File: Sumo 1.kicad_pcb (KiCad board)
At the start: 2 copper layers, 96.5 x 61 mm, 17 parts, among them J1 Trinket_Pro_5V, J2 SENSOR_CONN, J3 SENSOR_CONN, J4 SENSOR_CONN, M1 Motor_Connection, M2 Motor_Connection, M3 Motor_Connection, M4 Motor_Connection, U1 TB6612FNG

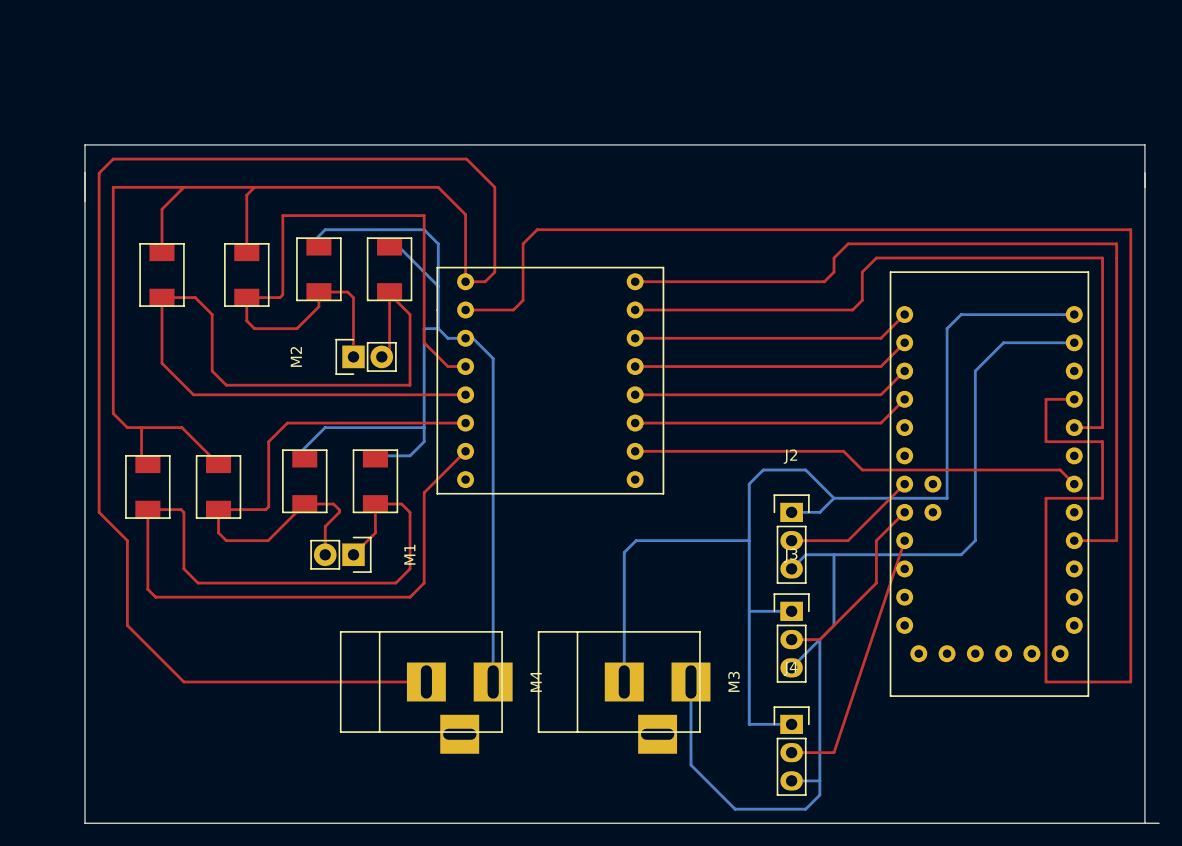
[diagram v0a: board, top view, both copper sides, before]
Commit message: First spin using bare SMT TB6612FNG.
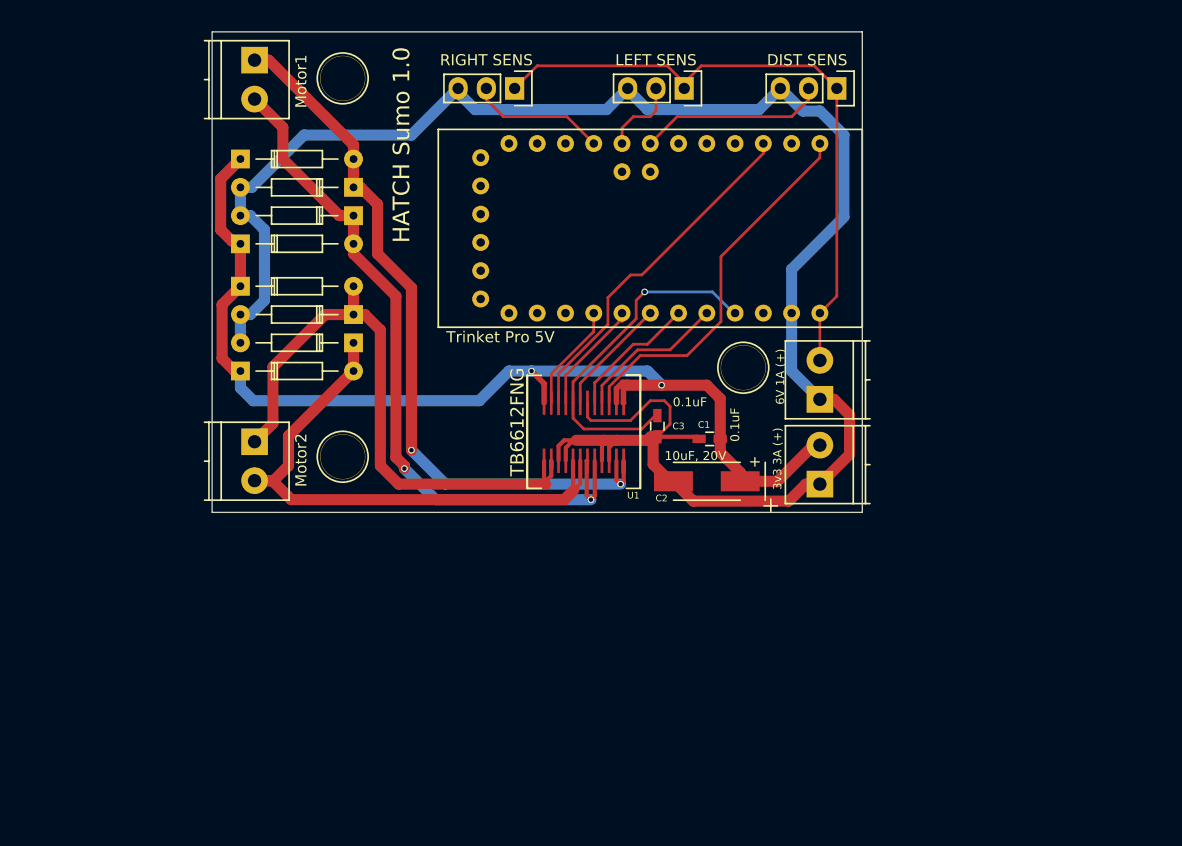
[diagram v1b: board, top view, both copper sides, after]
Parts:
- added ?: , Connect:1pin, F.Cu at (140.0, 122.0)
- added ?: , Connect:1pin, F.Cu at (176.0, 114.0)
- added ?: , Connect:1pin, F.Cu at (140.0, 88.0)
- added C1: 0.1uF, Capacitors_SMD:C_0603_HandSoldering, F.Cu at (173.0, 120.4)
- added C2: 10uF, 20V, Capacitors_Tantalum_SMD:TantalC_SizeC_EIA-6032_HandSoldering, F.Cu at (172.7, 124.2)
- added C3: 0.1uF, Capacitors_SMD:C_0603_HandSoldering, F.Cu at (168.3, 119.3)
- D1, D2, D3, D4, D5, D6, D7, D8: value D_Small -> 1N4001; footprint ArduinoFootprints:S1BB_rectifier_diode -> Diodes_ThroughHole:Diode_DO-35_SOD27_Horizontal_RM10
- J1: value Trinket_Pro_5V -> DIST SENS; footprint ArduinoFootprints:Trinket_Pro_5V -> Pin_Headers:Pin_Header_Straight_1x03
- J2: value SENSOR_CONN -> LEFT SENS
- J3: value SENSOR_CONN -> RIGHT SENS
- J4: value SENSOR_CONN -> Trinket Pro 5V; footprint Pin_Headers:Pin_Header_Straight_1x03 -> ArduinoFootprints:Trinket_Pro_5V
- M1: value Motor_Connection -> Logic Power; footprint Pin_Headers:Pin_Header_Straight_1x02 -> Terminal_Blocks:TerminalBlock_Pheonix_PT-3.5mm_2pol
- M2: value Motor_Connection -> Motor Power; footprint Pin_Headers:Pin_Header_Straight_1x02 -> Terminal_Blocks:TerminalBlock_Pheonix_PT-3.5mm_2pol
- M3: value Motor_Connection -> Motor1; footprint Connect:BARREL_JACK -> Terminal_Blocks:TerminalBlock_Pheonix_PT-3.5mm_2pol
- M4: value Motor_Connection -> Motor2; footprint Connect:BARREL_JACK -> Terminal_Blocks:TerminalBlock_Pheonix_PT-3.5mm_2pol
- U1: footprint ArduinoFootprints:TB6612FNG_motor_driver -> ArduinoFootprints:TB6612FNG
- moved M3 64.9 mm to (132.1, 86.4), turned to 270 degrees
- moved J4 53.8 mm to (186.7, 92.6), turned to 270 degrees
- moved J3 53.2 mm to (155.4, 88.9), turned to 270 degrees
- moved M1 44.2 mm to (182.9, 116.8), turned to 90 degrees
- moved M2 43.4 mm to (182.9, 124.5)
- moved J2 39.3 mm to (170.7, 88.9), turned to 270 degrees
- moved D2 29.2 mm to (141.0, 97.8), turned to 180 degrees
- moved D1 27.4 mm to (130.8, 95.2), turned to 0 degrees
- moved D4 27.4 mm to (141.0, 100.3), turned to 180 degrees
- moved M4 26.4 mm to (132.1, 120.7), turned to 270 degrees
- moved U1 19.8 mm to (161.7, 119.8)
- moved D3 19.0 mm to (130.8, 102.9), turned to 0 degrees
- moved J1 17.2 mm to (184.4, 88.9), turned to 270 degrees
- moved D7 12.5 mm to (130.8, 114.3), turned to 0 degrees
- moved D6 5.24 mm to (141.0, 109.2), turned to 180 degrees
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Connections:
- J1 pad 1: Net-(J1-Pad1) -> +6V
- J1 pad 3: /PWMA_W -> GND
- J2 pad 2: /DIST_SIGNAL -> /LEFT_SIGNAL
- J3 pad 2: /LEFT_SIGNAL -> /RIGHT_SIGNAL
- J4 pad 1: +6V -> Net-(J4-Pad1)
- J4 pad 3: GND -> /PWMA_W
- M1 pad 1: /B01_W -> GND
- M1 pad 2: /B02_W -> +6V
- M2 pad 1: /A01_W -> GND
- M2 pad 2: /A02_W -> +3V3
- M3 pad 1: GND -> /B01_W
- M3 pad 2: +6V -> /B02_W
- M4 pad 1: GND -> /A01_W
- M4 pad 2: +3V3 -> /A02_W
- U1 pad 1: +3V3 -> /A01_W
- U1 pad 10: /AIN2_W -> GND
- U1 pad 11: /AIN1_W -> /B01_W
- U1 pad 12: /STBY_W -> /B01_W
- U1 pad 13: /BIN1_W -> +3V3
- U1 pad 14: /BIN2_W -> +3V3
- U1 pad 16: Net-(U1-Pad16) -> /BIN2_W
- U1 pad 2: /V_LOGIC -> /A01_W
- U1 pad 4: /A01_W -> GND
- U1 pad 6: /B02_W -> /A02_W
- U1 pad 7: /B01_W -> /B02_W
- U1 pad 8: Net-(U1-Pad8) -> /B02_W
- U1 pad 9: /PWMA_W -> GND
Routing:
- net /V_LOGIC: track 152.1 -> 31.4 mm, vias 0 -> 1
- net +3V3: track 205.1 -> 98.0 mm, vias 0 -> 2
- net /PWMA_W: track 75.9 -> 9.65 mm
- net +6V: track 103.4 -> 57.5 mm
- net /AIN2_W: track 63.2 -> 31.5 mm
- net /A02_W: track 79.4 -> 52.5 mm
- net /B01_W: track 89.9 -> 67.6 mm, vias 0 -> 2
- net /B02_W: track 48.2 -> 64.8 mm, vias 0 -> 2
- net /STBY_W: track 25.1 -> 10.7 mm
- net /AIN1_W: track 25.1 -> 11.3 mm
- net /BIN1_W: track 25.1 -> 11.9 mm
- net /RIGHT_SIGNAL: track 23.9 -> 12.3 mm
- net /BIN2_W: track 25.1 -> 13.7 mm
- net GND: track 181.4 -> 171.1 mm
- net /LEFT_SIGNAL: track 17.1 -> 7.11 mm
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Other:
- board size 96.5 x 61 mm -> 58.4 x 43.2 mm
- net class MotorPower added: clearance 0.3, trace_width 0.75, via_dia 0.6, via_drill 0.4
- board text added: "(+)"
- board text added: "3v3 3A (+)"
- board text added: "6V 1A (+)"
- board text added: "HATCH Sumo 1.0"
- board text added: "HATCH Trinket Pro SumoBot v1.0, 21 July 2016 CC-BY-SA"
- board text added: "Logic Power – 6VDC 1A"
- board text added: "Motor Power 3.3VDC 3A"

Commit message: New spin!
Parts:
- added ?: , Diodes_ThroughHole:Diode_DO-35_SOD27_Horizontal_RM10, B.Cu at (141.0, 115.3)
- added ?: , Diodes_ThroughHole:Diode_DO-35_SOD27_Horizontal_RM10, B.Cu at (130.8, 117.9)
- added ?: , Diodes_ThroughHole:Diode_DO-35_SOD27_Horizontal_RM10, B.Cu at (141.0, 112.8)
- added ?: , Diodes_ThroughHole:Diode_DO-35_SOD27_Horizontal_RM10, B.Cu at (141.0, 98.0)
- added ?: , Diodes_ThroughHole:Diode_DO-35_SOD27_Horizontal_RM10, B.Cu at (130.8, 110.2)
- added ?: , Diodes_ThroughHole:Diode_DO-35_SOD27_Horizontal_RM10, B.Cu at (130.8, 100.6)
- added ?: , Diodes_ThroughHole:Diode_DO-35_SOD27_Horizontal_RM10, B.Cu at (141.0, 95.5)
- added ?: , Diodes_ThroughHole:Diode_DO-35_SOD27_Horizontal_RM10, B.Cu at (130.8, 93.2)
- added ?: , Connect:1pin, F.Cu at (183.0, 88.0)
- C1, C3: footprint Capacitors_SMD:C_0603_HandSoldering -> Capacitors_ThroughHole:C_Disc_D6_P5
- C2: footprint Capacitors_Tantalum_SMD:TantalC_SizeC_EIA-6032_HandSoldering -> Capacitors_ThroughHole:C_Disc_D6_P5
- moved M2 54.9 mm to (132.1, 103.6), turned to 270 degrees
- moved C1 27.8 mm to (146.3, 112.5), turned to 270 degrees
- moved ? 11.4 mm to (183.0, 123.0)
- moved C2 10.9 mm to (162.9, 119.4), turned to 270 degrees
- moved C3 10.2 mm to (163.1, 110.5)
- moved U1 8.50 mm to (153.7, 116.9)
- moved J1 6.73 mm to (177.8, 87.6)
- moved J2 4.87 mm to (166.0, 87.6)
- moved D5 3.56 mm to (130.8, 110.2)
- moved D6 3.56 mm to (141.0, 112.8)
- moved D7 3.56 mm to (130.8, 117.9)
- moved D8 3.56 mm to (141.0, 115.3)
- moved D2 2.29 mm to (141.0, 95.5)
- moved D3 2.29 mm to (130.8, 100.6)
- moved D4 2.29 mm to (141.0, 98.0)
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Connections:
- J1 pad 1: +6V -> /V_LOGIC
- J2 pad 1: +6V -> /V_LOGIC
- J3 pad 1: +6V -> /V_LOGIC
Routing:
- net GND: track 171.1 -> 80.9 mm
- net +6V: track 57.5 -> 6.03 mm
- net /V_LOGIC: track 31.4 -> 78.1 mm, vias 1 -> 0
- net /A01_W: track 55.1 -> 36.3 mm
- net /A02_W: track 52.5 -> 37.6 mm
- net /B01_W: track 67.6 -> 79.6 mm, vias 2 -> 0
- net /STBY_W: track 10.7 -> 22.2 mm
- net /PWMB_W: track 33.6 -> 44.2 mm
- net /BIN1_W: track 11.9 -> 21.1 mm
- net /BIN2_W: track 13.7 -> 22.7 mm
- net /PWMA_W: track 9.65 -> 18.7 mm
- net +3V3: track 98.0 -> 89.6 mm, vias 2 -> 0
- net /AIN2_W: track 31.5 -> 39.1 mm
- net /AIN1_W: track 11.3 -> 18.4 mm
- net /DIST_SIGNAL: track 16.9 -> 10.5 mm
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- added copper zone on B.Cu, net GND
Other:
- board text added: "+"
- board text added: "HATCH SumoBot 1.0 21 July 2016 CC-BY-SA"
- board text removed: "HATCH Sumo 1.0"

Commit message: Sumo v1 files
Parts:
- removed the ? at (141.0, 115.3)
- removed the ? at (140.0, 123.0)
- removed the ? at (183.0, 123.0)
- removed the ? at (140.0, 88.0)
- removed the ? at (130.8, 117.9)
- removed the ? at (141.0, 112.8)
- removed the ? at (141.0, 98.0)
- removed the ? at (130.8, 110.2)
- removed the ? at (130.8, 100.6)
- removed the ? at (141.0, 95.5)
- removed the ? at (130.8, 93.2)
- removed the ? at (183.0, 88.0)
- removed the C1 at (146.3, 112.5)
- removed the C2 at (162.9, 119.4)
- removed the C3 at (163.1, 110.5)
- removed the D1 at (130.8, 93.2)
- removed the D2 at (141.0, 95.5)
- removed the D3 at (130.8, 100.6)
- removed the D4 at (141.0, 98.0)
- removed the D5 at (130.8, 110.2)
- removed the D6 at (141.0, 112.8)
- removed the D7 at (130.8, 117.9)
- removed the D8 at (141.0, 115.3)
- removed J2: LEFT SENS, Pin_Headers:Pin_Header_Straight_1x03
- removed J3: RIGHT SENS, Pin_Headers:Pin_Header_Straight_1x03
- removed J4: Trinket Pro 5V, ArduinoFootprints:Trinket_Pro_5V
- removed the M1 at (182.9, 116.8)
- removed the M2 at (132.1, 103.6)
- removed M3: Motor1, Terminal_Blocks:TerminalBlock_Pheonix_PT-3.5mm_2pol
- removed M4: Motor2, Terminal_Blocks:TerminalBlock_Pheonix_PT-3.5mm_2pol
- added ?: , Connect:1pin, F.Cu at (114.8, 136.1)
- added ?: , Pin_Headers:Pin_Header_Straight_1x02, F.Cu at (162.3, 99.4)
- added ?: , Connect:1pin, F.Cu at (114.8, 100.1)
- added ?: DIST SENS, Pin_Headers:Pin_Header_Straight_1x03, F.Cu at (114.8, 116.1)
- added ?: LEFT SENS, Pin_Headers:Pin_Header_Straight_1x03, F.Cu at (114.8, 106.2)
- added ?: RIGHT SENS, Pin_Headers:Pin_Header_Straight_1x03, F.Cu at (114.8, 126.0)
- added ?: LED1, Pin_Headers:Pin_Header_Straight_1x03, F.Cu at (119.6, 109.0)
- added ?: LED2, Pin_Headers:Pin_Header_Straight_1x02, F.Cu at (119.6, 118.9)
- added ?: , Connect:1pin, F.Cu at (167.6, 100.3)
- added ?: , Pin_Headers:Pin_Header_Straight_1x02, F.Cu at (123.2, 99.4)
- added C1: 0.1uF, Capacitors_ThroughHole:C_Rect_L7_W3.5_P5, B.Cu at (147.6, 103.6)
- added C1: , Capacitors_ThroughHole:C_Rect_L7_W3.5_P5, F.Cu at (147.6, 98.6)
- added C2: 10uF, 20V, Capacitors_ThroughHole:C_Radial_D5_L6_P2.5, B.Cu at (153.2, 100.3)
- added C2: , Capacitors_ThroughHole:C_Radial_D5_L6_P2.5, F.Cu at (153.2, 100.3)
- added C3: 0.1uF, Capacitors_ThroughHole:C_Rect_L7_W3.5_P5, B.Cu at (147.8, 122.2)
- added C3: , Capacitors_ThroughHole:C_Rect_L7_W3.5_P5, F.Cu at (147.8, 117.1)
- added C4: 10uF, 20V, Capacitors_ThroughHole:C_Radial_D5_L6_P2.5, B.Cu at (153.2, 117.1)
- added C4: , Capacitors_ThroughHole:C_Radial_D5_L6_P2.5, F.Cu at (153.2, 117.1)
- added D1: , Diodes_ThroughHole:Diode_DO-35_SOD27_Horizontal_RM10, B.Cu at (161.8, 118.1)
- added D1: , Diodes_ThroughHole:Diode_DO-35_SOD27_Horizontal_RM10, F.Cu at (161.8, 118.1)
- added D2: , Diodes_ThroughHole:Diode_DO-35_SOD27_Horizontal_RM10, B.Cu at (159.0, 108.0)
- added D2: , Diodes_ThroughHole:Diode_DO-35_SOD27_Horizontal_RM10, F.Cu at (159.0, 108.0)
- added D3: , Diodes_ThroughHole:Diode_DO-35_SOD27_Horizontal_RM10, B.Cu at (159.0, 120.9)
- added D3: , Diodes_ThroughHole:Diode_DO-35_SOD27_Horizontal_RM10, F.Cu at (159.0, 120.9)
- added D4: , Diodes_ThroughHole:Diode_DO-35_SOD27_Horizontal_RM10, B.Cu at (169.2, 123.4)
- added D4: , Diodes_ThroughHole:Diode_DO-35_SOD27_Horizontal_RM10, F.Cu at (169.2, 123.4)
- added D5: , Diodes_ThroughHole:Diode_DO-35_SOD27_Horizontal_RM10, B.Cu at (147.6, 127.3)
- added D5: , Diodes_ThroughHole:Diode_DO-35_SOD27_Horizontal_RM10, F.Cu at (147.6, 127.3)
- added D6: , Diodes_ThroughHole:Diode_DO-35_SOD27_Horizontal_RM10, B.Cu at (157.7, 129.8)
- added D6: , Diodes_ThroughHole:Diode_DO-35_SOD27_Horizontal_RM10, F.Cu at (157.7, 129.8)
- added D7: , Diodes_ThroughHole:Diode_DO-35_SOD27_Horizontal_RM10, B.Cu at (147.6, 132.3)
- added D7: , Diodes_ThroughHole:Diode_DO-35_SOD27_Horizontal_RM10, F.Cu at (147.6, 132.3)
- added D8: D1-8: 1N4001, Diodes_ThroughHole:Diode_DO-35_SOD27_Horizontal_RM10, B.Cu at (157.7, 134.9)
- added D8: , Diodes_ThroughHole:Diode_DO-35_SOD27_Horizontal_RM10, F.Cu at (157.7, 134.9)
- added EXP: , Pin_Headers:Pin_Header_Straight_1x08, F.Cu at (124.2, 116.3)
- added LPWR1: Logic Power, Terminal_Blocks:TerminalBlock_Pheonix_PT-3.5mm_2pol, B.Cu at (120.1, 101.6)
- added LPWR1: Logic Power, Terminal_Blocks:TerminalBlock_Pheonix_PT-3.5mm_2pol, F.Cu at (123.7, 101.6)
- added M1: Motor1, Terminal_Blocks:TerminalBlock_Pheonix_PT-3.5mm_2pol, B.Cu at (166.4, 110.0)
- added M1: Motor 1, Terminal_Blocks:TerminalBlock_Pheonix_PT-3.5mm_2pol, F.Cu at (166.4, 113.5)
- added M2: , Terminal_Blocks:TerminalBlock_Pheonix_PT-3.5mm_2pol, B.Cu at (166.4, 127.8)
- added M2: Motor 2, Terminal_Blocks:TerminalBlock_Pheonix_PT-3.5mm_2pol, F.Cu at (166.4, 131.3)
- added MPWR1: Motor Power, Terminal_Blocks:TerminalBlock_Pheonix_PT-3.5mm_2pol, B.Cu at (159.3, 101.6)
- added MPWR1: Motor Pwr, Terminal_Blocks:TerminalBlock_Pheonix_PT-3.5mm_2pol, F.Cu at (162.8, 101.6)
- added P1: , Pin_Headers:Pin_Header_Straight_1x03, B.Cu at (114.8, 116.1)
- added P2: , Pin_Headers:Pin_Header_Straight_1x03, B.Cu at (114.8, 106.2)
- added P3: , Pin_Headers:Pin_Header_Straight_1x03, B.Cu at (114.8, 126.0)
- added P4: , Pin_Headers:Pin_Header_Straight_1x03, B.Cu at (119.6, 109.0)
- added P5: , Pin_Headers:Pin_Header_Straight_1x02, B.Cu at (119.6, 118.9)
- added REF**: 1pin, Connect:1pin, F.Cu at (167.6, 136.1)
- added XP1: EXP, Pin_Headers:Pin_Header_Straight_1x08, B.Cu at (124.2, 116.3)
- J1: value DIST SENS -> Trinket_Pro_5V; footprint Pin_Headers:Pin_Header_Straight_1x03 -> ArduinoFootprints:Trinket_Pro_5V
- U1: moved to B.Cu
- moved J1 52.5 mm to (126.7, 99.8), turned to 0 degrees
- moved U1 7.33 mm to (150.6, 110.2), turned to 270 degrees
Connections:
- net +3V3 renamed V_MOTOR
- net /A01_W renamed A01
- net /A02_W renamed A02
- net /B01_W renamed B01
- net /B02_W renamed B02
- J1 pad 1: /V_LOGIC -> RST
- J1 pad 3: GND -> LED1_RED
- U1 pad 10: GND -> GND_LOGIC
- U1 pad 15: /PWMB_W -> PWMB
- U1 pad 16: /BIN2_W -> BIN2
- U1 pad 17: /BIN1_W -> BIN1
- U1 pad 18: GND -> GND_LOGIC
- U1 pad 19: /STBY_W -> STBY
- U1 pad 20: /V_LOGIC -> V_LOGIC
- U1 pad 21: /AIN1_W -> AIN1
- U1 pad 22: /AIN2_W -> AIN2
- U1 pad 23: /PWMA_W -> PWMA
- U1 pad 3: GND -> GND_LOGIC
- U1 pad 4: GND -> GND_LOGIC
- U1 pad 9: GND -> GND_LOGIC
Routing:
- net GND: track 80.9 -> 0.00 mm
- net /V_LOGIC: track 78.1 -> 0.00 mm
- net /PWMB_W: track 44.2 -> 0.00 mm
- net B01: track 79.6 -> 36.2 mm
- net V_LOGIC: track 0.00 -> 42.7 mm
- net PWMB: track 0.00 -> 41.1 mm, vias 0 -> 1
- net /AIN2_W: track 39.1 -> 0.00 mm
- net LED1_RED: track 0.00 -> 36.5 mm, vias 0 -> 1
- net B02: track 66.2 -> 33.0 mm
- net LED2: track 0.00 -> 27.9 mm
- net V_MOTOR: track 89.6 -> 64.2 mm
- net GND_LOGIC: track 0.00 -> 23.9 mm
- net SENS_LEFT: track 0.00 -> 22.9 mm
- net /BIN2_W: track 22.7 -> 0.00 mm
- net V_BAT: track 0.00 -> 22.6 mm
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- added copper zone on F.Cu, net GND_LOGIC
- added copper zone on B.Cu, net V_LOGIC
- added copper zone on B.Cu, net V_MOTOR
- removed copper zone on B.Cu, net GND
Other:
- board size 58.4 x 43.2 mm -> 59.9 x 42.9 mm
- net class MotorPower removed
- board text added: "3v3"
- board text added: "5V"
- board text added: "6V"
- board text added: "A4"
- board text added: "A5"
- board text added: "AREF"
- board text added: "D1-8 are 1N4001 or equivalent. Be careful of polarity for C2, C4, and diodes! Smaller power pads are for JST or pin headers; larger for terminal blocks."
- board text added: "DIST"
- board text added: "GND"
- board text added: "GRN"
- board text added: "HATCH Sumo v1"
- board text added: "LEFT"
- board text added: "RED"
- board text added: "RIGHT"
- board text added: "RST"
- board text added: "RX"
- board text added: "TX"
- board text added: "Trinket Pro 5V"
- board text added: "©2016 WFPL CC-BY-NC-SA"
- board text added: "©2016 WFPL CC-BY-NC-SA Logic Power: 6VDC @ 1mA Motor Power: 3.3VDC @ 3A LED1 and 2 can drive 20mA at 5VDC."
- board text removed: "(+)"
- board text removed: "3v3 3A (+)"
- board text removed: "6V 1A (+)"
- board text removed: "HATCH SumoBot 1.0 21 July 2016 CC-BY-SA"
- board text removed: "HATCH Trinket Pro SumoBot v1.0, 21 July 2016 CC-BY-SA"
- board text removed: "Logic Power – 6VDC 1A"
- board text removed: "Motor Power 3.3VDC 3A"
